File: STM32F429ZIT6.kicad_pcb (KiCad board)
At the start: 4 copper layers, 112.2 x 85.6 mm, 117 parts, among them J2 Conn_01x05_Pin, P1 Header 32X2, P2 Header 32X2, SW1 K3-1235S, U2 LD3985M33R, U3 MCP6004, U4 NAU88C22YG_C914209, U5 RCLAMP0521P.TCT_C3029033, U6 RCLAMP0521P.TCT_C3029033, U7 W9825G6KH-6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

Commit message: didnt save?
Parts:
- moved C55 0.14 mm to (174.8, 107.5)
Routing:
- net /PG8: track 22.3 -> 72.0 mm, vias 2 -> 3
- net /PG7: track 9.87 -> 59.2 mm
- net /PG6: track 13.2 -> 57.1 mm
- net /A6: track 18.7 -> 55.1 mm, vias 0 -> 1
- net /A7: track 24.2 -> 57.4 mm
- net /A5: track 19.8 -> 50.7 mm, vias 1 -> 2
- net /A4: track 22.0 -> 50.3 mm, vias 1 -> 2
- net /BA1: track 48.9 -> 75.3 mm
- net /BA0: track 47.5 -> 72.0 mm
- net /A10: track 24.4 -> 41.9 mm, vias 2 -> 3
- net /PF11: track 38.9 -> 48.3 mm
- net /SWO: track 27.7 -> 20.7 mm
- net /A12: track 15.1 -> 22.2 mm, vias 3 -> 4
- net /PB6: track 30.1 -> 32.4 mm, vias 3 -> 2
- net /PC0: track 25.5 -> 23.4 mm
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
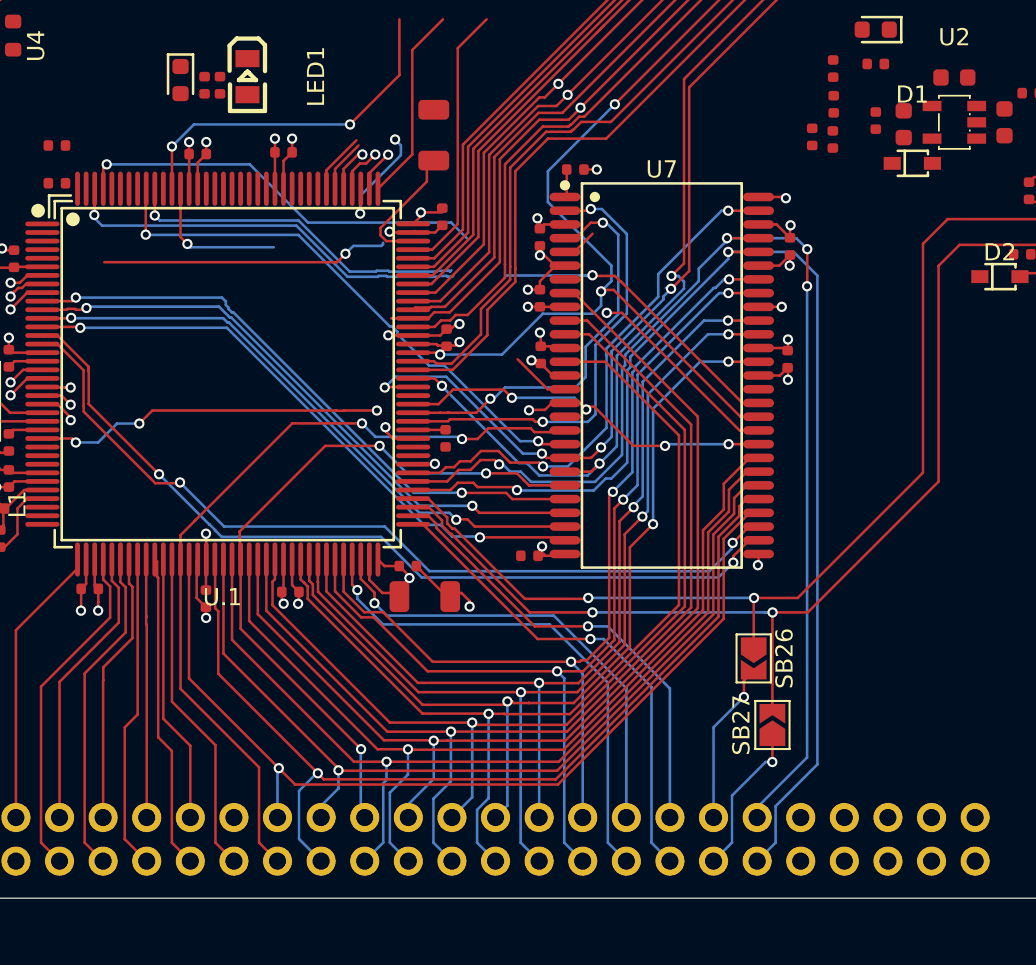
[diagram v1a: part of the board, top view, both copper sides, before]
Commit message: i think sdram is all connected+brokenout
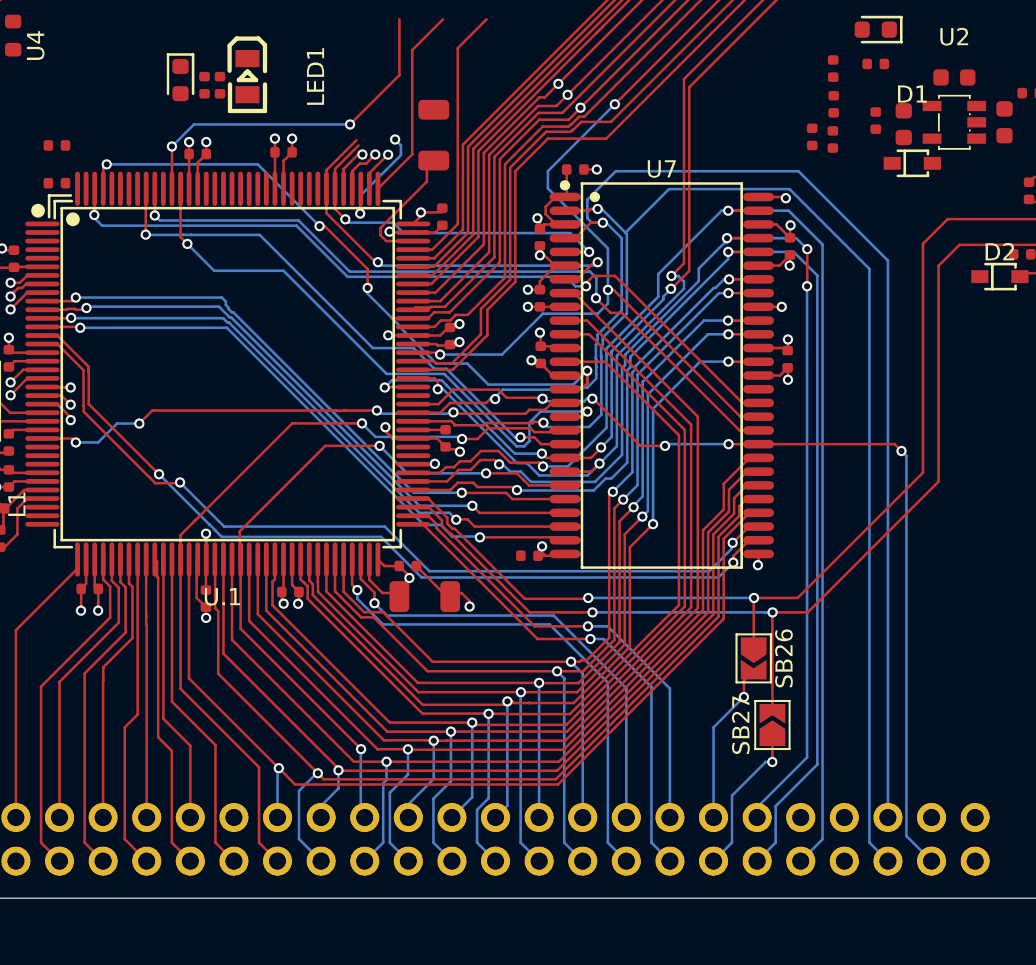
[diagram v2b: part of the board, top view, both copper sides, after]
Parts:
- moved C21 0.22 mm to (170.2, 94.7)
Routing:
- net /D1: track 24.0 -> 79.4 mm
- net /D0: track 26.6 -> 79.3 mm
- net /D15: track 31.7 -> 74.5 mm
- net /A12: track 22.2 -> 55.3 mm, vias 4 -> 5
- net /PG15: track 9.25 -> 35.2 mm, vias 1 -> 2
- net /D3: track 4.09 -> 25.1 mm, vias 0 -> 2
- net /D2: track 5.14 -> 22.2 mm, vias 0 -> 2
- net /SWDIO: track 33.5 -> 16.7 mm, vias 1 -> 0
- net /NBL0: track 27.8 -> 39.0 mm, vias 1 -> 4
- net /PB5: track 32.5 -> 43.2 mm
- net /PC0: track 23.4 -> 32.4 mm
- net /NBL1: track 42.0 -> 45.5 mm
- net +3.3V: track 47.7 -> 50.9 mm
- net GND: track 60.4 -> 63.5 mm, vias 24 -> 25

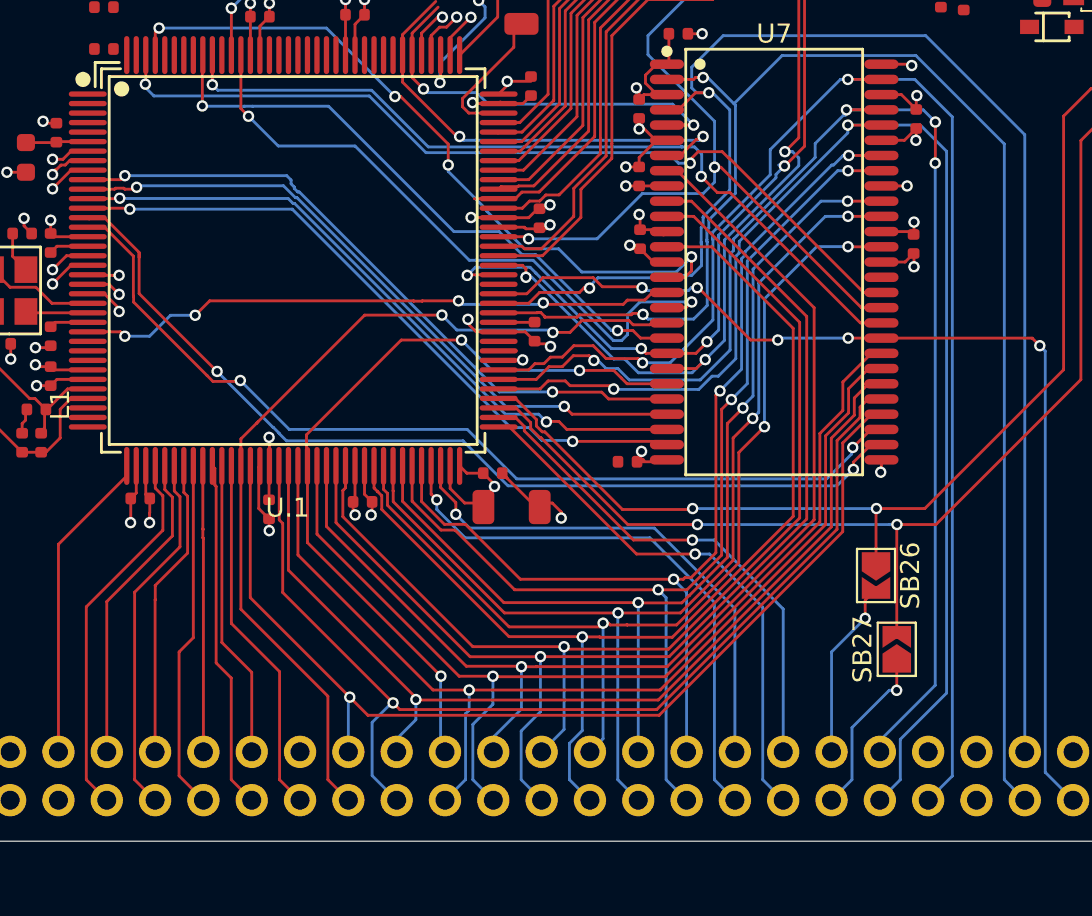
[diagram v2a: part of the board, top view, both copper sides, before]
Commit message: broke out pb13 12 and 11. they are not used by anything yet
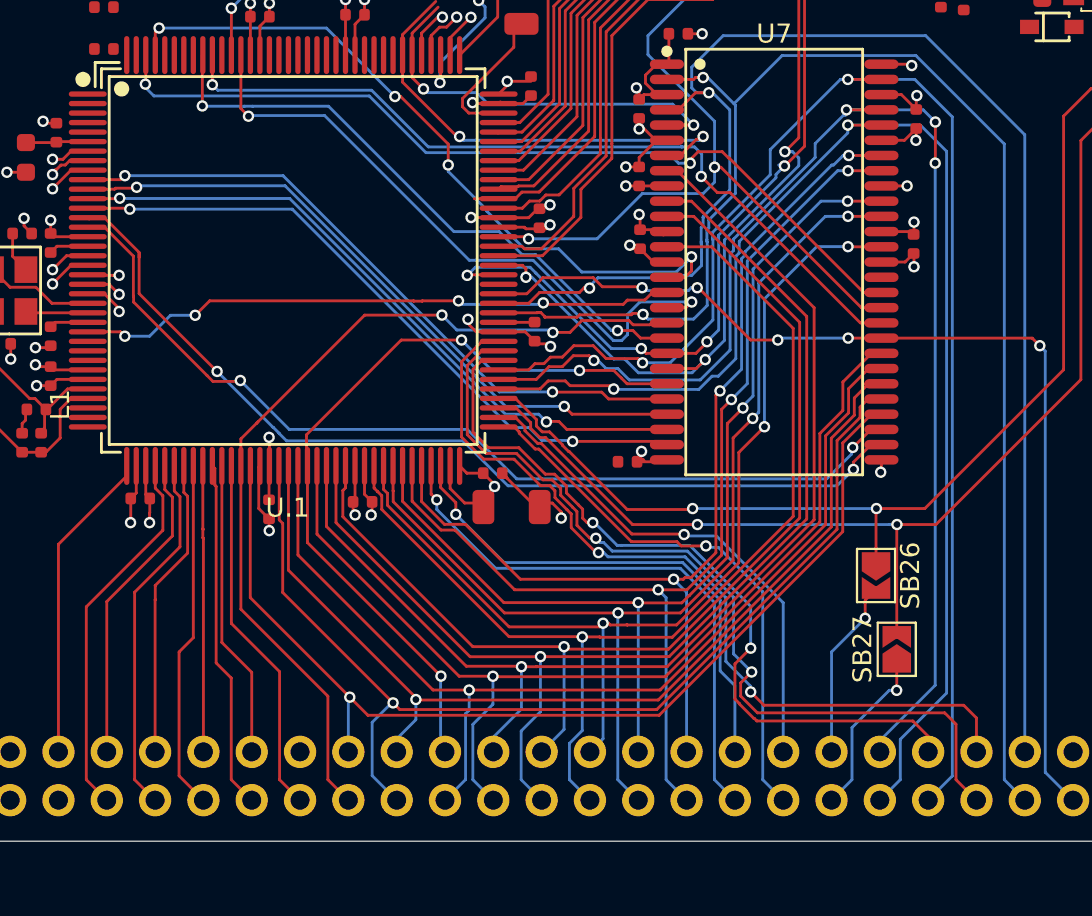
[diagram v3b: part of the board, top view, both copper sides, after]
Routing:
- net /PD12: track 1.81 -> 47.0 mm, vias 0 -> 2
- net /PD13: track 0.83 -> 44.9 mm, vias 0 -> 2
- net /PD11: track 2.15 -> 40.9 mm, vias 1 -> 2

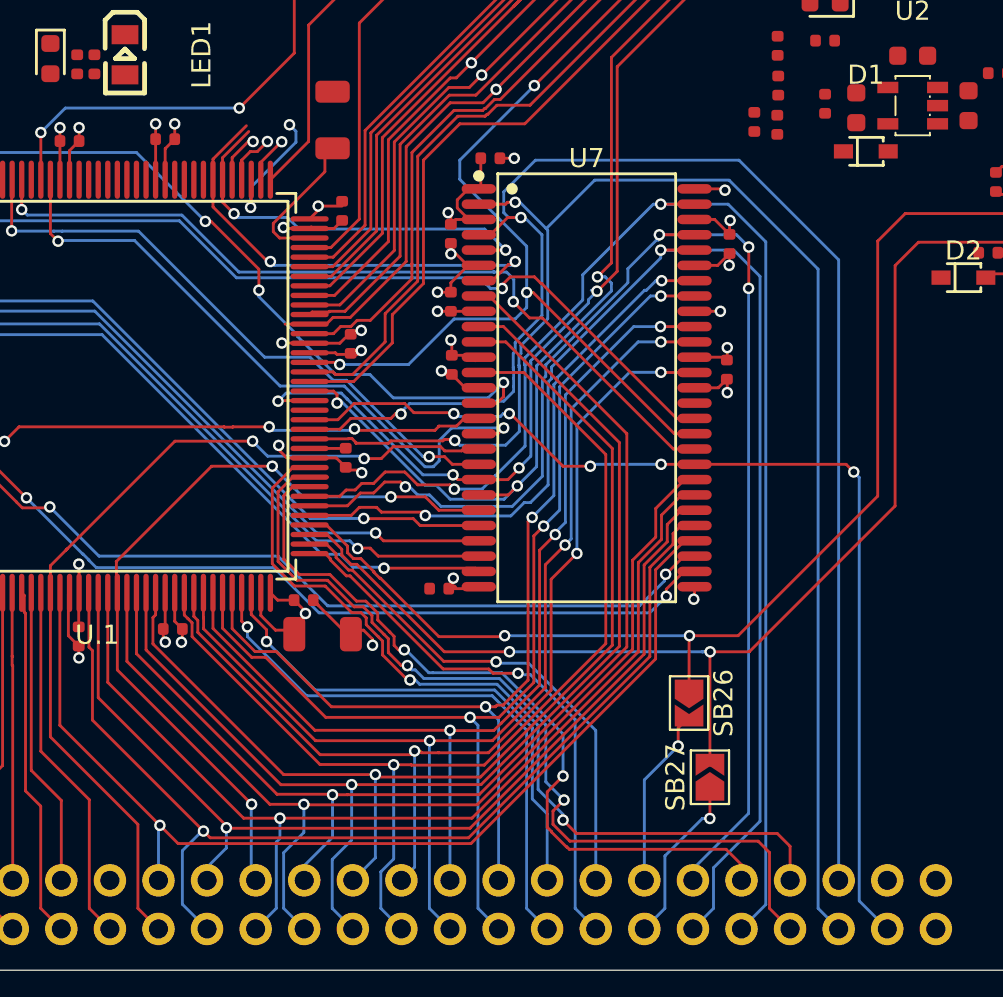
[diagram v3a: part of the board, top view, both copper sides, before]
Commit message: pg3 breakout also not connected to anything
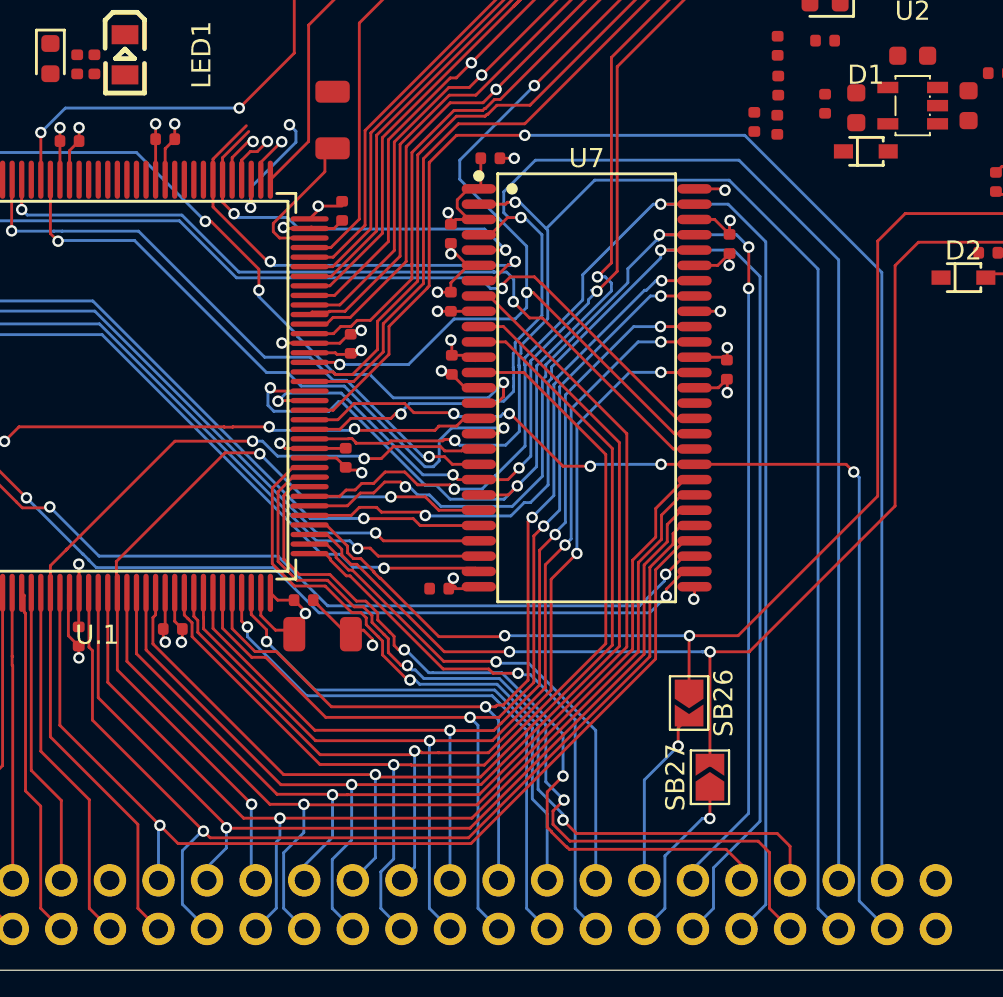
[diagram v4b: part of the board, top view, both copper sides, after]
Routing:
- net /PG3: track 0.00 -> 75.4 mm, vias 0 -> 1
- net /BA1: track 75.6 -> 80.6 mm
- net GND: track 63.5 -> 61.3 mm, vias 25 -> 24
- net +3.3V: track 50.9 -> 52.6 mm, vias 18 -> 19
- net /I2S_MCK: track 52.0 -> 50.7 mm
- net /A10: track 41.9 -> 42.4 mm

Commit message: closer to breakout done, need to wire codec now
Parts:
- moved C39 96.1 mm to (37.8, 69.5)
- moved C49 96.1 mm to (46.2, 73.7)
- moved C50 96.1 mm to (47.8, 67.2)
- moved C51 96.1 mm to (42.2, 63.2)
- moved C52 96.1 mm to (42.0, 65.2)
- moved R11 96.1 mm to (37.8, 73.0)
- moved R17 96.1 mm to (48.9, 70.4)
- moved U4 96.1 mm to (42.7, 69.4)
- moved C48 96.1 mm to (42.2, 74.2)
- moved L2 96.1 mm to (39.0, 63.2)
- moved R18 96.1 mm to (43.8, 75.8)
- moved H1 84.3 mm to (12.6, -29.6)
- moved H2 84.3 mm to (12.6, -21.6)
- moved H3 84.3 mm to (12.6, -13.7)
- moved H4 84.3 mm to (12.6, -5.75)
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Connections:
- J2 pad 2: /SWDIO -> /PA13
- J2 pad 3: /SWCLK -> /PA14
- J2 pad 4: /SWO -> /PB3
- U.1 pad 105: /SWDIO -> /PA13
- U.1 pad 109: /SWCLK -> /PA14
- U.1 pad 133: /SWO -> /PB3
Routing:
- net /PB3: track 0.00 -> 86.4 mm, vias 0 -> 3
- net /PA14: track 0.00 -> 62.3 mm, vias 0 -> 1
- net /PA13: track 0.00 -> 62.3 mm, vias 0 -> 1
- net /A4: track 50.3 -> 99.5 mm, vias 2 -> 4
- net /A5: track 50.7 -> 97.0 mm, vias 2 -> 4
- net /BOOT0: track 0.50 -> 45.4 mm
- net /A3: track 36.2 -> 80.3 mm, vias 2 -> 3
- net /A2: track 35.8 -> 79.6 mm
- net /A0: track 35.4 -> 77.6 mm
- net /A1: track 35.5 -> 75.4 mm
- net /PC14: track 2.31 -> 40.6 mm, vias 1 -> 0
- net /PC15: track 2.26 -> 39.2 mm, vias 1 -> 0
- net /PE6: track 0.00 -> 35.8 mm
- net /PE4: track 0.00 -> 33.5 mm
- net /PC13: track 2.03 -> 34.6 mm, vias 1 -> 0
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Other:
- board size 112.2 x 85.6 mm -> 107.8 x 68.5 mm
- board text added: "stm32f429zit6 dev board sdram + audio codec test aidan swank 2026"
- board text removed: "fffffffffffff"

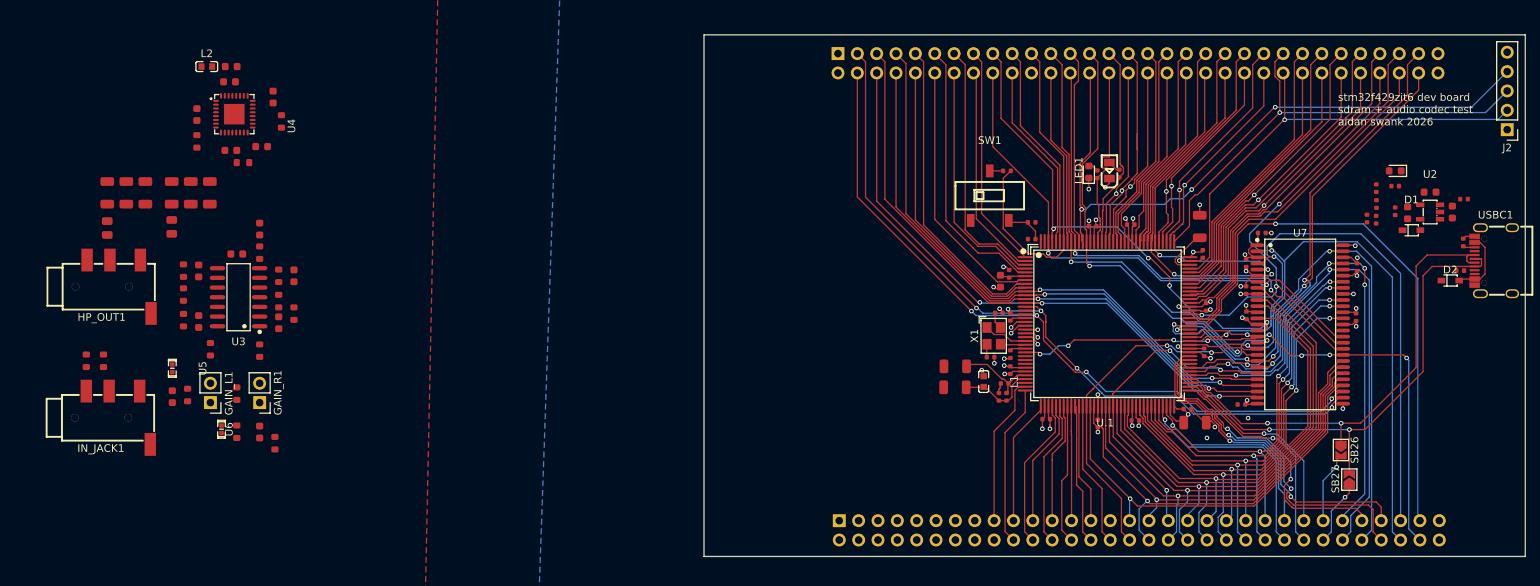
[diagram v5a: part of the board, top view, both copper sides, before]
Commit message: esd protection for usb data lines
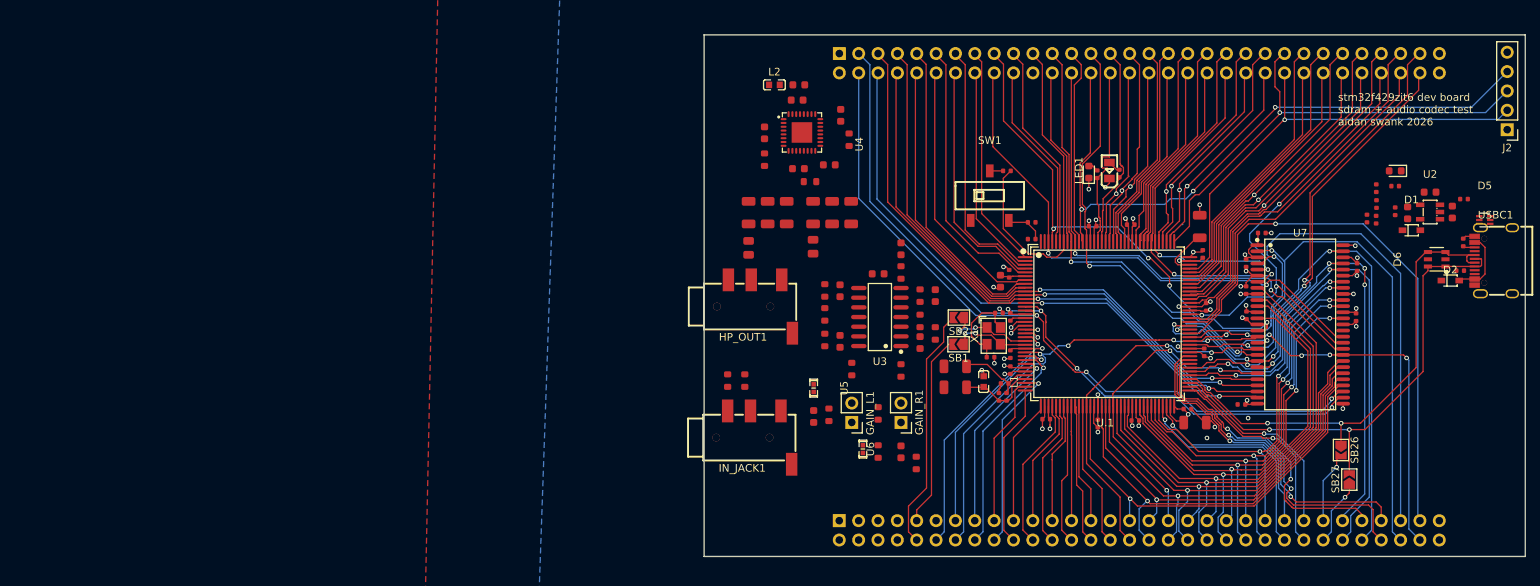
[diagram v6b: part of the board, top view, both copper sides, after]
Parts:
- added D5: USBLC6-2P6, easyeda2kicad:SOT-666-6_L1.6-W1.2-P0.50-LS1.6-BR, F.Cu at (206.8, 83.3)
- added D6: USBLC6-2SC6, easyeda2kicad:SOT-23-6_L2.9-W1.6-P0.95-LS2.8-BL, F.Cu at (200.4, 88.5)
- added SB1: Circuit Breaker, Jumper:SolderJumper-2_P1.3mm_Open_TrianglePad1.0x1.5mm, F.Cu at (137.7, 99.6)
- added SB2: Circuit Breaker, Jumper:SolderJumper-2_P1.3mm_Open_TrianglePad1.0x1.5mm, F.Cu at (137.8, 96.1)
- moved C33 84.2 mm to (132.7, 99.4)
- moved C35 84.2 mm to (130.2, 113.7)
- moved C36 84.2 mm to (122.2, 92.6)
- moved C37 84.2 mm to (122.2, 99.2)
- moved C38 84.2 mm to (134.7, 93.2)
- moved C40 84.2 mm to (130.2, 87.1)
- moved C41 84.2 mm to (127.2, 90.4)
- moved C45 84.2 mm to (110.2, 82.3)
- moved C46 84.2 mm to (112.7, 82.3)
- moved C47 84.2 mm to (115.2, 82.3)
- moved GAIN_R1 84.2 mm to (130.2, 109.9)
- moved R10 84.2 mm to (132.7, 93.2)
- moved R12 84.2 mm to (130.2, 90.2)
- moved R13 84.2 mm to (132.7, 96.5)
- moved R14 84.2 mm to (134.7, 98.2)
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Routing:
- net /NRST: track 2.05 -> 35.7 mm, vias 0 -> 1
- net /PH0: track 0.00 -> 32.1 mm
- net /PC0: track 33.1 -> 63.5 mm
- net /PC1: track 0.00 -> 29.3 mm, vias 0 -> 1
- net /PC2: track 0.00 -> 29.2 mm, vias 0 -> 1
- net /PH1: track 0.00 -> 25.4 mm
- net /PC3: track 0.00 -> 25.3 mm, vias 0 -> 1
- net /PA0: track 0.00 -> 24.7 mm, vias 0 -> 1
- net Net-(C30-Pad1): track 3.91 -> 11.7 mm
- net /OSC_OUT: track 3.28 -> 9.84 mm, vias 0 -> 2
- net /OSC_IN: track 5.74 -> 11.2 mm, vias 0 -> 2
- net /PG11: track 28.7 -> 26.9 mm
- net /PB15: track 61.8 -> 63.2 mm
- net /A4: track 99.5 -> 99.3 mm, vias 4 -> 3
- net /A3: track 80.3 -> 80.4 mm, vias 3 -> 2
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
